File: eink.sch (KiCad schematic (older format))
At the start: 20 parts, among them P301 eInk, Q301 IRLML0030TRPBF

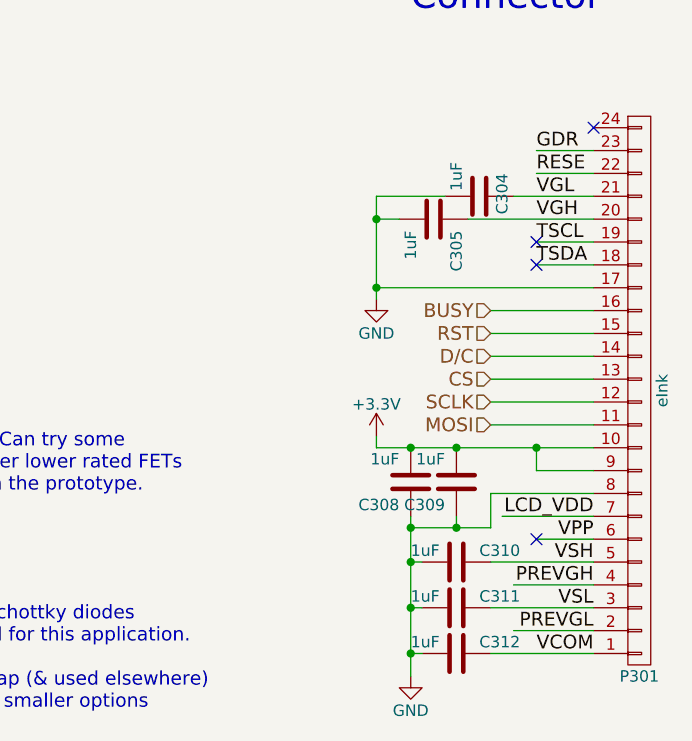
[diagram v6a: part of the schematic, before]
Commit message: Add SZLCSC part links
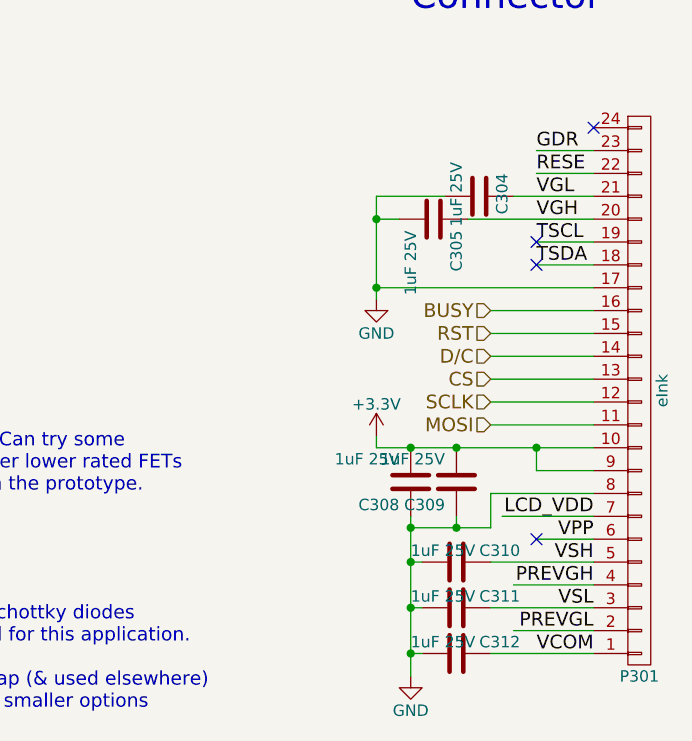
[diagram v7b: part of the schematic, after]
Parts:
- C301: LCSC (none) -> http://www.szlcsc.com/product/details_94382.html
- C302, C303: LCSC (none) -> http://www.szlcsc.com/product/details_16531.html
- C304, C305, C308, C309, C310, C311, C312: value 1uF -> 1uF 25V; LCSC (none) -> http://www.szlcsc.com/product/details_94382.html
- C306: footprint Capacitors_SMD:C_0603_HandSoldering -> Capacitors_SMD:C_0805_HandSoldering; LCSC (none) -> http://www.szlcsc.com/product/details_107126.html
- C307: LCSC (none) -> http://www.szlcsc.com/product/details_42881.html
- D301, D302, D303: LCSC (none) -> http://www.szlcsc.com/product/details_110425.html
- L301: LCSC (none) -> http://www.szlcsc.com/product/details_61593.html
- P301: LCSC (none) -> http://www.szlcsc.com/product/details_11604.html
- Q301: LCSC (none) -> http://www.szlcsc.com/product/details_68364.html
- R301: LCSC (none) -> http://www.szlcsc.com/product/details_16080.html
- R302: LCSC (none) -> http://www.szlcsc.com/product/details_24144.html
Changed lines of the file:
@@
 F 2 "libs:FPC_0.5mm_Pitch_24_Pin" H 7900 4000 50  0001 C CNN
 F 3 "" H 7900 4000 50  0000 C CNN
+F 4 "http://www.szlcsc.com/product/details_11604.html" H 7350 2250 60  0001 C CNN "LCSC"
 	1    7900 4000
 	1    0    0    1
@@
 P 7200 3150
 F 0 "C304" H 7100 3250 50  0000 L CNN
-F 1 "1uF" H 7050 3050 50  0000 L CNN
+F 1 "1uF 25V" H 7050 3050 50  0000 L CNN
 F 2 "Capacitors_SMD:C_0603_HandSoldering" H 7238 3000 50  0001 C CNN
 F 3 "" H 7200 3150 50  0000 C CNN
+F 4 "http://www.szlcsc.com/product/details_94382.html" H 7350 2250 60  0001 C CNN "LCSC"
 	1    7200 3150
 	0    1    1    0
@@
 P 7000 3250
 F 0 "C305" H 7050 3350 50  0000 L CNN
-F 1 "1uF" H 7050 3150 50  0000 L CNN
+F 1 "1uF 25V" H 7050 3150 50  0000 L CNN
 F 2 "Capacitors_SMD:C_0603_HandSoldering" H 7038 3100 50  0001 C CNN
 F 3 "" H 7000 3250 50  0000 C CNN
+F 4 "http://www.szlcsc.com/product/details_94382.html" H 7350 2250 60  0001 C CNN "LCSC"
 	1    7000 3250
 	0    1    1    0
@@
 P 6900 4400
 F 0 "C308" H 6950 4500 50  0000 L CNN
-F 1 "1uF" H 6950 4300 50  0000 L CNN
+F 1 "1uF 25V" H 6950 4300 50  0000 L CNN
 F 2 "Capacitors_SMD:C_0603_HandSoldering" H 6938 4250 50  0001 C CNN
 F 3 "" H 6900 4400 50  0000 C CNN
+F 4 "http://www.szlcsc.com/product/details_94382.html" H 7350 2250 60  0001 C CNN "LCSC"
 	1    6900 4400
 	-1   0    0    1
@@
 P 7100 4400
 F 0 "C309" H 7150 4500 50  0000 L CNN
-F 1 "1uF" H 7150 4300 50  0000 L CNN
+F 1 "1uF 25V" H 7150 4300 50  0000 L CNN
 F 2 "Capacitors_SMD:C_0603_HandSoldering" H 7138 4250 50  0001 C CNN
 F 3 "" H 7100 4400 50  0000 C CNN
+F 4 "http://www.szlcsc.com/product/details_94382.html" H 7350 2250 60  0001 C CNN "LCSC"
 	1    7100 4400
 	-1   0    0    1
@@
 P 7100 4750
 F 0 "C310" V 7050 4850 50  0000 L CNN
-F 1 "1uF" V 7050 4550 50  0000 L CNN
+F 1 "1uF 25V" V 7050 4550 50  0000 L CNN
 F 2 "Capacitors_SMD:C_0603_HandSoldering" H 7138 4600 50  0001 C CNN
 F 3 "" H 7100 4750 50  0000 C CNN
+F 4 "http://www.szlcsc.com/product/details_94382.html" H 7350 2250 60  0001 C CNN "LCSC"
 	1    7100 4750
 	0    1    1    0
@@
 P 7100 4950
 F 0 "C311" V 7050 5050 50  0000 L CNN
-F 1 "1uF" V 7050 4750 50  0000 L CNN
+F 1 "1uF 25V" V 7050 4750 50  0000 L CNN
 F 2 "Capacitors_SMD:C_0603_HandSoldering" H 7138 4800 50  0001 C CNN
 F 3 "" H 7100 4950 50  0000 C CNN
+F 4 "http://www.szlcsc.com/product/details_94382.html" H 7350 2250 60  0001 C CNN "LCSC"
 	1    7100 4950
 	0    1    1    0
@@
 P 7100 5150
 F 0 "C312" V 7050 5250 50  0000 L CNN
-F 1 "1uF" V 7050 4950 50  0000 L CNN
+F 1 "1uF 25V" V 7050 4950 50  0000 L CNN
 F 2 "Capacitors_SMD:C_0603_HandSoldering" H 7138 5000 50  0001 C CNN
 F 3 "" H 7100 5150 50  0000 C CNN
+F 4 "http://www.szlcsc.com/product/details_94382.html" H 7350 2250 60  0001 C CNN "LCSC"
 	1    7100 5150
 	0    1    1    0
@@
 F 6 "RC0603FR-0712KL" V -7900 2550 60  0001 C CNN "Manufacturer PN"
 F 7 "0.10" V -7900 2550 60  0001 C CNN "Unit Cost"
+F 8 "http://www.szlcsc.com/product/details_16080.html" H 7350 2250 60  0001 C CNN "LCSC"
 	1    1500 1150
 	0    -1   -1   0
@@
 F 2 "Capacitors_SMD:C_0603_HandSoldering" H 1788 1250 50  0001 C CNN
 F 3 "" H 1750 1400 50  0000 C CNN
+F 4 "http://www.szlcsc.com/product/details_94382.html" H 7350 2250 60  0001 C CNN "LCSC"
 	1    1750 1400
 	-1   0    0    1
@@
 F 2 "Capacitors_SMD:C_0805_HandSoldering" H 3088 4050 50  0001 C CNN
 F 3 "" H 3050 4200 50  0001 C CNN
+F 4 "http://www.szlcsc.com/product/details_42881.html" H 7350 2250 60  0001 C CNN "LCSC"
 	1    3050 4200
 	1    0    0    -1
@@
 F 5 "587-3070-1-ND" V 3350 3950 60  0001 C CNN "Digikey PN"
 F 6 "FIXED IND 68UH 410MA 1.3 OHM 1210 SMD" V 3350 3950 60  0001 C CNN "Description"
+F 7 "http://www.szlcsc.com/product/details_61593.html" H 7350 2250 60  0001 C CNN "LCSC"
 	1    3350 3950
 	0    -1   -1   0
@@
 F 2 "Diodes_SMD:D_SOD-323" H 3650 3300 50  0001 C CNN
 F 3 "" H 3650 3300 50  0001 C CNN
+F 4 "http://www.szlcsc.com/product/details_110425.html" H 7350 2250 60  0001 C CNN "LCSC"
 	1    3650 3300
 	0    1    1    0
@@
 F 2 "Capacitors_SMD:C_0603_HandSoldering" H 3288 2850 50  0001 C CNN
 F 3 "" H 3250 3000 50  0001 C CNN
+F 4 "http://www.szlcsc.com/product/details_16531.html" H 7350 2250 60  0001 C CNN "LCSC"
 	1    3250 3000
 	0    1    1    0
@@
 F 2 "Diodes_SMD:D_SOD-323" H 4250 3300 50  0001 C CNN
 F 3 "" H 4250 3300 50  0001 C CNN
+F 4 "http://www.szlcsc.com/product/details_110425.html" H 7350 2250 60  0001 C CNN "LCSC"
 	1    4250 3300
 	0    1    1    0
@@
 F 2 "Capacitors_SMD:C_0603_HandSoldering" H 4588 2850 50  0001 C CNN
 F 3 "" H 4550 3000 50  0001 C CNN
+F 4 "http://www.szlcsc.com/product/details_16531.html" H 7350 2250 60  0001 C CNN "LCSC"
 	1    4550 3000
 	0    1    1    0
@@
 F 2 "Diodes_SMD:D_SOD-323" H 4850 3300 50  0001 C CNN
 F 3 "" H 4850 3300 50  0001 C CNN
+F 4 "http://www.szlcsc.com/product/details_110425.html" H 7350 2250 60  0001 C CNN "LCSC"
 	1    4850 3300
 	0    -1   -1   0
@@
 F 0 "C306" H 4575 3850 50  0000 L CNN
 F 1 "4.7uF 50V" H 4150 3850 50  0000 L CNN
-F 2 "Capacitors_SMD:C_0603_HandSoldering" H 4588 3600 50  0001 C CNN
+F 2 "Capacitors_SMD:C_0805_HandSoldering" H 4588 3600 50  0001 C CNN
 F 3 "" H 4550 3750 50  0001 C CNN
+F 4 "http://www.szlcsc.com/product/details_107126.html" H 7350 2250 60  0001 C CNN "LCSC"
 	1    4550 3750
 	-1   0    0    1
@@
 F 2 "Resistors_SMD:R_0603_HandSoldering" V 4130 4700 50  0001 C CNN
 F 3 "" H 4200 4700 50  0001 C CNN
+F 4 "http://www.szlcsc.com/product/details_24144.html" H 7350 2250 60  0001 C CNN "LCSC"
 	1    4200 4700
 	1    0    0    -1
@@
 F 2 "TO_SOT_Packages_SMD:SOT-23" H 4500 4300 50  0001 C CNN
 F 3 "" H 4300 4200 50  0001 C CNN
+F 4 "http://www.szlcsc.com/product/details_68364.html" H 7350 2250 60  0001 C CNN "LCSC"
 	1    4300 4200
 	-1   0    0    -1
